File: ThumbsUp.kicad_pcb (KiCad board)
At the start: 2 copper layers, 282 x 464.4 mm, 159 parts, among them J19 52559-1233, J32 Battery, SW2 SW_DIP_x01, U1 ProMicro

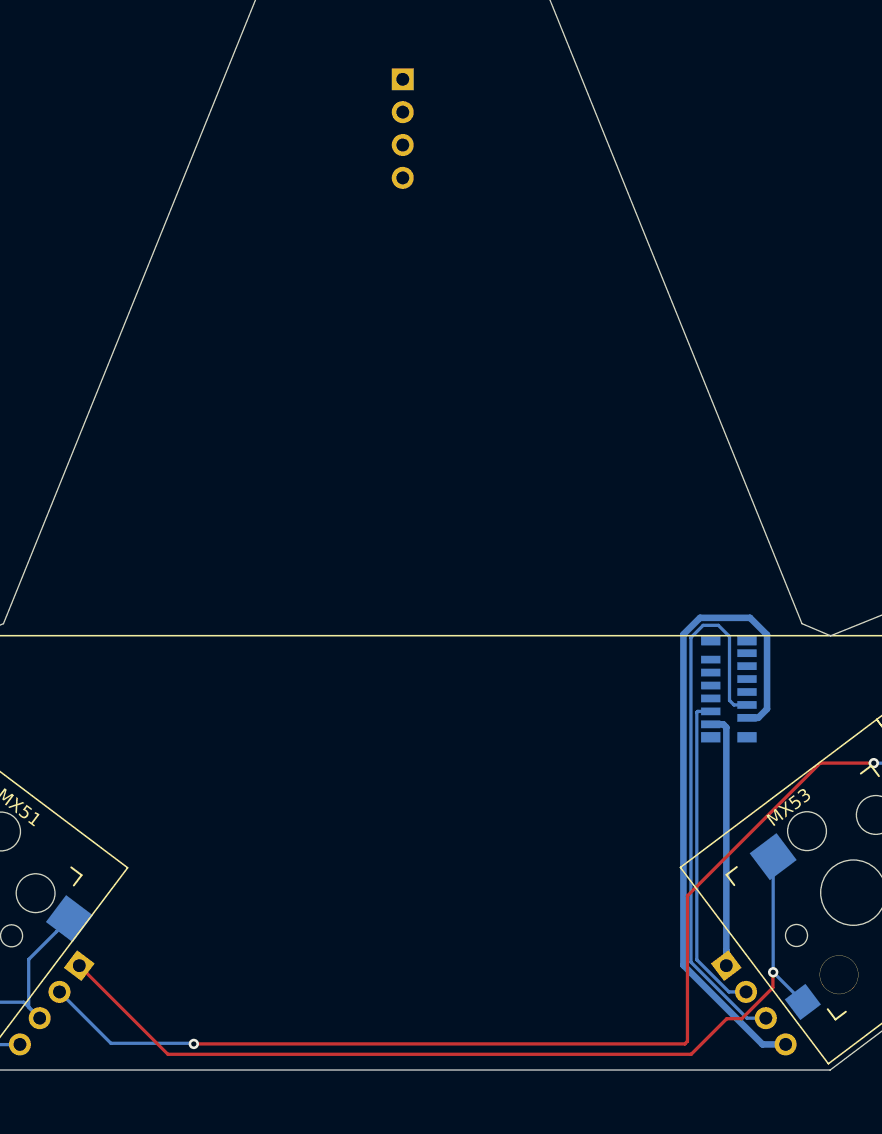
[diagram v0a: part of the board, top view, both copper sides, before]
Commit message: Wired all levels
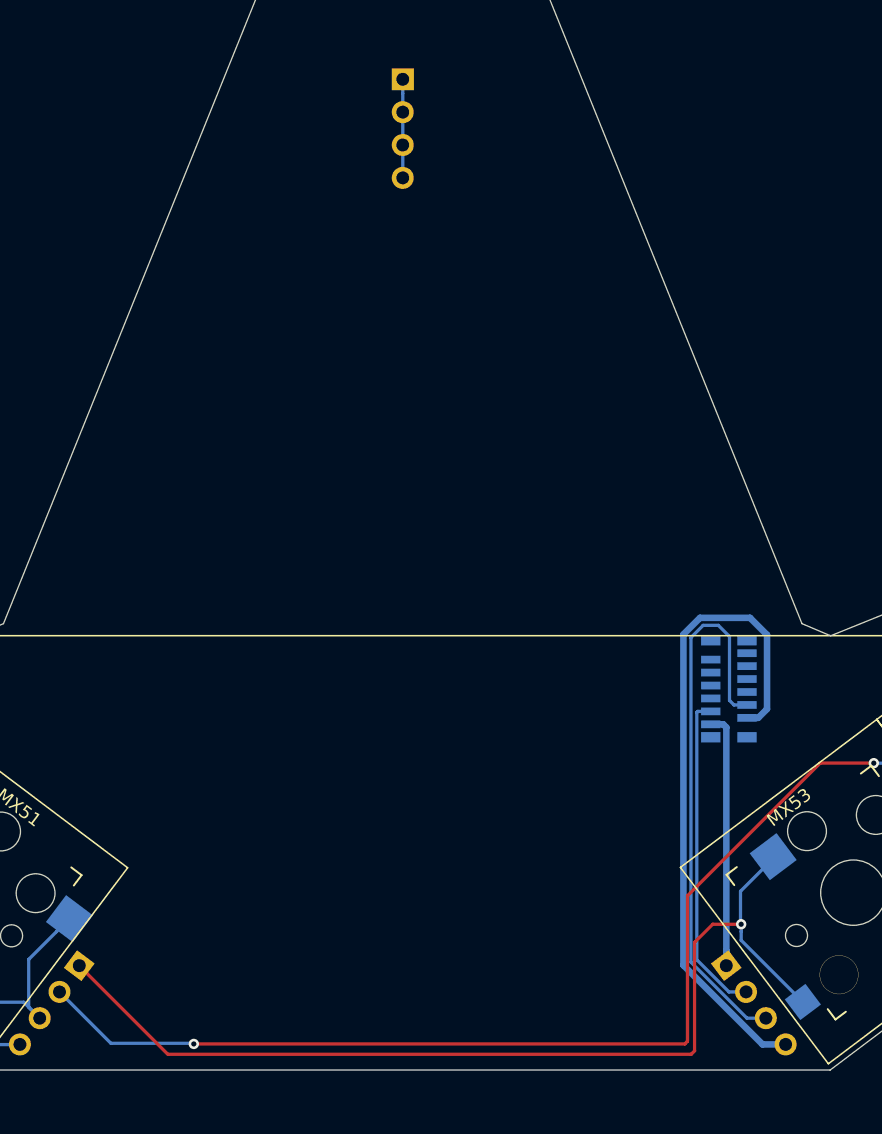
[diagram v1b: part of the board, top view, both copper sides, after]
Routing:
- net L3GND: track 0.00 -> 7.62 mm
- net Net-(JM45-Pad1): track 71.9 -> 77.3 mm
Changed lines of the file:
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@@
     (thickness 1.6)
     (drawings 115)
-    (tracks 2164)
+    (tracks 2170)
     (zones 0)
     (modules 159)
@@
     (add_net "Net-(D8-Pad2)")
     (add_net "Net-(D9-Pad2)")
-    (add_net "Net-(J19-Pad1)")
-    (add_net "Net-(J19-Pad2)")
-    (add_net "Net-(J19-Pad3)")
-    (add_net "Net-(J19-Pad4)")
-    (add_net "Net-(J19-Pad5)")
-    (add_net "Net-(J19-Pad6)")
-    (add_net "Net-(J19-Pad7)")
-    (add_net "Net-(J19-Pad8)")
-    (add_net "Net-(J19-PadMP1)")
-    (add_net "Net-(J19-PadMP2)")
-    (add_net "Net-(J19-PadMP3)")
-    (add_net "Net-(J19-PadMP4)")
-    (add_net "Net-(JF11-Pad1)")
     (add_net "Net-(JF20-Pad1)")
     (add_net "Net-(JF20-Pad2)")
@@
   (segment (start -286.6 117.35) (end -290.75 117.35) (width 0.254) (layer F.Cu) (net 129))
   (segment (start -290.75 117.35) (end -301 127.6) (width 0.254) (layer F.Cu) (net 129))
-  (segment (start -294.375654 133.510851) (end -294.375654 124.576541) (width 0.254) (layer B.Cu) (net 130))
-  (segment (start -292.080148 135.806357) (end -294.375654 133.510851) (width 0.254) (layer B.Cu) (net 130))
-  (via (at -294.375654 133.510851) (size 0.8) (drill 0.4) (layers F.Cu B.Cu) (net 130))
-  (segment (start -341.15 139.85) (end -348 133) (width 0.254) (layer F.Cu) (net 130))
-  (segment (start -294.375654 133.510851) (end -294.4 133.535197) (width 0.254) (layer F.Cu) (net 130))
-  (segment (start -294.4 134.699106) (end -296.800894 137.1) (width 0.254) (layer F.Cu) (net 130))
-  (segment (start -296.800894 137.1) (end -297.964803 137.1) (width 0.254) (layer F.Cu) (net 130))
-  (segment (start -294.4 133.535197) (end -294.4 134.699106) (width 0.254) (layer F.Cu) (net 130))
-  (segment (start -297.964803 137.1) (end -300.714803 139.85) (width 0.254) (layer F.Cu) (net 130))
-  (segment (start -300.714803 139.85) (end -341.15 139.85) (width 0.254) (layer F.Cu) (net 130))
+  (segment (start -296.85 131.036505) (end -296.85 130.365685) (width 0.254) (layer B.Cu) (net 130))
+  (segment (start -296.85 130.365685) (end -296.85 129.8) (width 0.254) (layer B.Cu) (net 130))
+  (segment (start -292.080148 135.806357) (end -296.85 131.036505) (width 0.254) (layer B.Cu) (net 130))
+  (via (at -296.85 129.8) (size 0.8) (drill 0.4) (layers F.Cu B.Cu) (net 130))
+  (segment (start -296.9 129.75) (end -296.85 129.8) (width 0.254) (layer B.Cu) (net 130))
+  (segment (start -296.9 127.25) (end -296.9 129.75) (width 0.254) (layer B.Cu) (net 130))
+  (segment (start -294.375654 124.576541) (end -294.375654 124.725654) (width 0.254) (layer B.Cu) (net 130))
+  (segment (start -294.375654 124.725654) (end -296.9 127.25) (width 0.254) (layer B.Cu) (net 130))
+  (segment (start -299.05 129.8) (end -296.85 129.8) (width 0.254) (layer F.Cu) (net 130))
+  (segment (start -300.45 131.2) (end -299.05 129.8) (width 0.254) (layer F.Cu) (net 130))
+  (segment (start -300.45 139.585197) (end -300.45 131.2) (width 0.254) (layer F.Cu) (net 130))
+  (segment (start -300.714803 139.85) (end -300.45 139.585197) (width 0.254) (layer F.Cu) (net 130))
+  (segment (start -348 133) (end -341.15 139.85) (width 0.254) (layer F.Cu) (net 130))
+  (segment (start -341.15 139.85) (end -300.714803 139.85) (width 0.254) (layer F.Cu) (net 130))
+  (segment (start -323 65.604) (end -323 72.12) (width 0.254) (layer B.Cu) (net 132))
+  (segment (start -323 64.5) (end -323 65.604) (width 0.254) (layer B.Cu) (net 132))
   (via (at -278.7 296.8) (size 0.8) (drill 0.4) (layers F.Cu B.Cu) (net 133))
   (segment (start -278.61539 297.8) (end -278.61539 296.88461) (width 0.254) (layer B.Cu) (net 133))
